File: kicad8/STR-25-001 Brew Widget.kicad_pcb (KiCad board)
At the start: 4 copper layers, 25 x 94 mm, 71 parts, among them J1 USB_B_Micro, Q1 IRLML6401, Q2 FS8205A, SW1 BOOT, SW2 RESET, U1 ESP32-C3-MINI-1-N4, U2 TP4057, U3 MT3608, U4 MPU-6500, U5 MAX17048, U6 DS18B20U, U7 DW01A

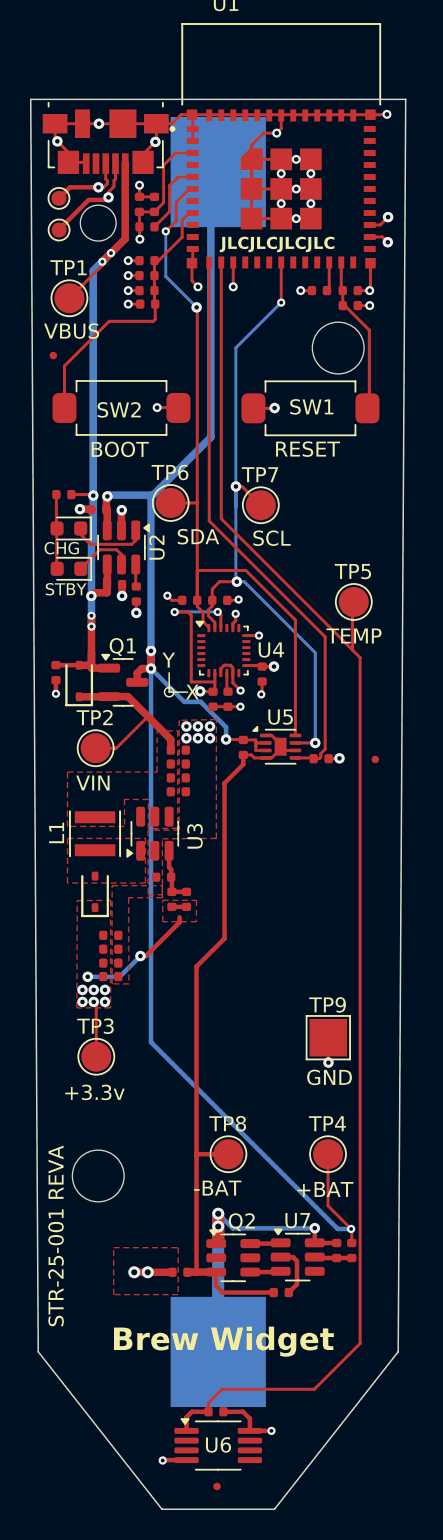
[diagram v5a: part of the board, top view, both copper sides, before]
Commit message: Finalising deisgn, first checks review done
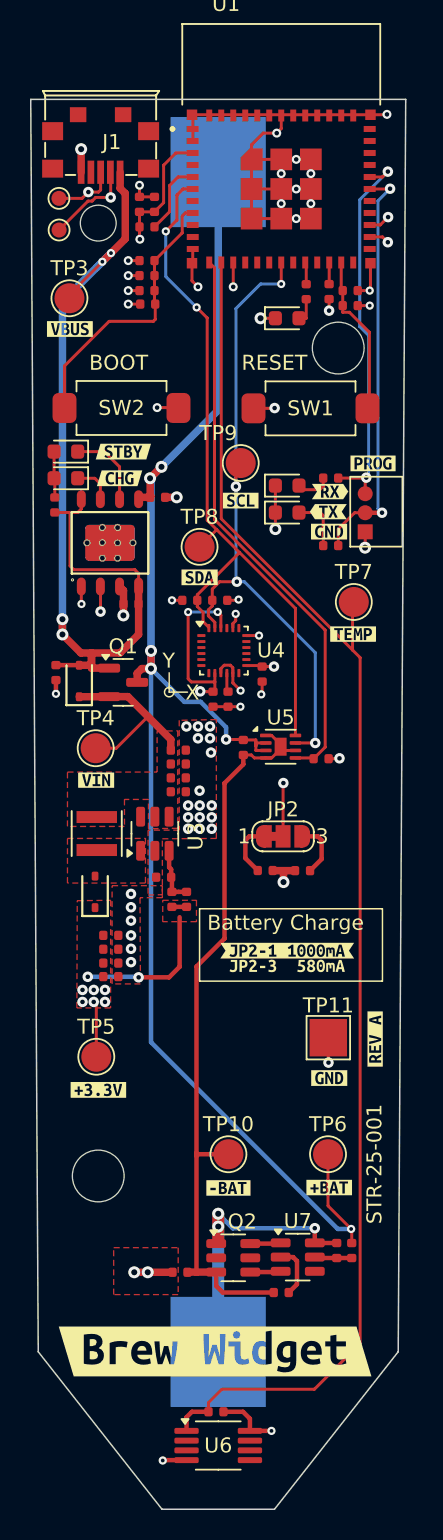
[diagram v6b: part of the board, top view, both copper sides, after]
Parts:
- removed FID1, FID2, FID3: Fiducial, Fiducial:Fiducial_0.5mm_Mask1mm
- removed PN1: ~, JLCPCB-Kicad-Footprints:Part_Num_JLCPCB
- added D5: RED, LED_SMD:LED_0603_1608Metric, F.Cu at (149.1, 85.3)
- added D6: RED, LED_SMD:LED_0603_1608Metric, F.Cu at (149.1, 96.5)
- added D7: RED, LED_SMD:LED_0603_1608Metric, F.Cu at (149.1, 98.3)
- added JP2: SolderJumper_3_Bridged12, Jumper:SolderJumper-3_P1.3mm_Bridged12_RoundedPad1.0x1.5mm_NumberLabels, F.Cu at (148.8, 119.9)
- added PROG1: Pogo Pin 1.27mm, STR-Footprints:PROG_1x3_1.27, F.Cu at (154.3, 99.6)
- added R18: 1.2kΩ, JLCPCB-Kicad-Footprints:R_0402, F.Cu at (147.6, 122.2)
- added R19: 1.5kΩ, JLCPCB-Kicad-Footprints:R_0402, F.Cu at (150.4, 83.6)
- added R20: 1.5kΩ, JLCPCB-Kicad-Footprints:R_0402, F.Cu at (152.0, 96.0)
- added R21: 1.5kΩ, JLCPCB-Kicad-Footprints:R_0402, F.Cu at (152.0, 100.5)
- added kibuzzard-67834543: G***, kibuzzard-67834543, F.Cu at (151.9, 136.0)
- added kibuzzard-67834564: G***, kibuzzard-67834564, F.Cu at (136.5, 136.8)
- added kibuzzard-6783457B: G***, kibuzzard-6783457B, F.Cu at (151.9, 143.3)
- added kibuzzard-67834594: G***, kibuzzard-67834594, F.Cu at (145.2, 143.3)
- added kibuzzard-678345AF: G***, kibuzzard-678345AF, F.Cu at (153.5, 106.4)
- added kibuzzard-678345CB: G***, kibuzzard-678345CB, F.Cu at (136.4, 116.1)
- added kibuzzard-678345D9: G***, kibuzzard-678345D9, F.Cu at (143.3, 102.6)
- added kibuzzard-678345E8: G***, kibuzzard-678345E8, F.Cu at (146.0, 97.5)
- added kibuzzard-67834607: G***, kibuzzard-67834607, F.Cu at (134.6, 86.1)
- added kibuzzard-678346A0: G***, kibuzzard-678346A0, F.Cu at (144.3, 154.2)
- added kibuzzard-67834787: G***, kibuzzard-67834787, F.Cu at (155.0, 133.4)
- added kibuzzard-67835DB7: G***, kibuzzard-67835DB7, F.Cu at (151.9, 99.6)
- added kibuzzard-67835E03: G***, kibuzzard-67835E03, F.Cu at (152.0, 96.9)
- added kibuzzard-67835E0F: G***, kibuzzard-67835E0F, F.Cu at (151.8, 98.2)
- added kibuzzard-67835E3B: G***, kibuzzard-67835E3B, F.Cu at (154.8, 95.0)
- added kibuzzard-67836539: G***, kibuzzard-67836539, F.Cu at (138.2, 94.2)
- added kibuzzard-67836544: G***, kibuzzard-67836544, F.Cu at (137.9, 96.0)
- added kibuzzard-67837AE8: G***, kibuzzard-67837AE8, F.Cu at (149.1, 127.5)
- added kibuzzard-67837E72: G***, kibuzzard-67837E72, F.Cu at (149.1, 128.5)
- C11: value 4.7uF -> 10uF
- J1: footprint Connector_USB:USB_Micro-B_Molex_47346-0001 -> STR-Footprints:MICRO-USB-SMD_5P_C40945
- L1: footprint STR-Passive:IND_LQH3NPZ220MMEL -> STR-Footprints:IND_LQH3NPZ220MMEL
- SW1, SW2: footprint STR-Switch:SW_SMD_SPST_8x3.6 -> STR-Footprints:SW_SMD_SPST_8x3.6
- U1: footprint STR-ESP32:ESP32-C3-MINI-1-N4 -> STR-Footprints:ESP32-C3-MINI-1-N4
- U2: value TP4057 -> TP4056; footprint Package_TO_SOT_SMD:TSOT-23-6 -> STR-Footprints:ESOP-8_L4.9-W3.9-P1.27-LS6.0-BL-EP
- moved R10 21.5 mm to (150.1, 122.2), turned to 180 degrees
- moved D3 7.82 mm to (134.3, 94.2)
- moved C15 4.01 mm to (140.5, 97.3), turned to 0 degrees
- moved TP8 3.50 mm to (143.3, 100.6)
- moved D2 3.35 mm to (134.3, 96.0)
- moved TP9 3.12 mm to (146.0, 95.0)
- moved C11 1.70 mm to (138.7, 104.4), turned to 180 degrees
- moved R9 0.92 mm to (133.6, 97.8), turned to 90 degrees
- moved U2 0.83 mm to (137.3, 100.3), turned to 0 degrees
- moved R7 0.65 mm to (151.9, 83.6), turned to 90 degrees
- moved J1 0.36 mm to (136.7, 73.7), turned to -90 degrees
- moved L1 0.11 mm to (136.4, 119.7)
- renumbered TP11 to TP1, TP8 to TP10, TP9 to TP11, TP10 to TP2, TP1 to TP3, TP2 to TP4, TP3 to TP5, TP4 to TP6, TP5 to TP7, TP6 to TP8, TP7 to TP9
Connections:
- D2 pad 1: Net-(D2-K) -> /~{CHG}
- D3 pad 1: Net-(D3-K) -> /~{STBY}
- R10 pad 1: Net-(U2-PROG) -> Net-(JP2-B)
- U1 pad 20: unconnected-(U1-IO6-Pad20) -> GPIO6
- U1 pad 30: unconnected-(U1-IO20/RXD0-Pad30) -> TX_IN
- U1 pad 31: unconnected-(U1-IO21/TXD0-Pad31) -> RX_IN
- U2 pad 1: Net-(D2-K) -> GND
- U2 pad 2: GND -> /PROG
- U2 pad 3: +BATT -> GND
- U2 pad 5: Net-(D3-K) -> +BATT
- U2 pad 6: Net-(U2-PROG) -> /~{STBY}
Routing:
- net TX_IN: track 0.00 -> 27.9 mm, vias 0 -> 2
- net RX_IN: track 0.00 -> 25.8 mm, vias 0 -> 2
- net /PROG: track 0.00 -> 24.5 mm, vias 0 -> 2
- net VBUS: track 49.5 -> 64.8 mm, vias 6 -> 4
- net GND: track 91.0 -> 82.6 mm, vias 40 -> 57
- net /~{STBY}: track 0.00 -> 5.37 mm
- net Net-(D2-K): track 5.12 -> 0.00 mm
- net Net-(D3-K): track 4.03 -> 0.00 mm
- net Net-(JP2-B): track 0.00 -> 3.73 mm
- net Net-(D7-A): track 0.00 -> 3.70 mm
- net Net-(JP2-A): track 0.00 -> 3.68 mm
- net /~{CHG}: track 0.00 -> 2.69 mm
- net Net-(D6-A): track 0.00 -> 2.26 mm
- net +BATT: track 105.2 -> 103.0 mm, vias 5 -> 6
- net Net-(D2-A): track 4.99 -> 3.08 mm
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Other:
- board text added: "Battery Charge"
- board text added: "STR-25-001"
- board text removed: "+3.3v"
- board text removed: "+BAT"
- board text removed: "-"
- board text removed: "-BAT"
- board text removed: "Brew Widget"
- board text removed: "CHG"
- board text removed: "GND"
- board text removed: "SCL"
- board text removed: "SDA"
- board text removed: "STBY"
- board text removed: "STR-25-001 REVA"
- board text removed: "TEMP"
- board text removed: "VBUS"
- board text removed: "VIN"

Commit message: BOM generated
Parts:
- removed the R16 at (141.9, 148.9)
- added R20: 0Ω, JLCPCB-Kicad-Footprints:R_0805, F.Cu at (141.3, 149.0)
- D5: renamed from D2; value CHG -> RED
- D6: renamed from D3; value STBY -> GREEN
- SW1: value BOOT -> SPST 8x3.6
- SW2: value RESET -> SPST 8x3.6
- moved D5 0.56 mm to (134.9, 96.0)
- moved D6 0.56 mm to (134.9, 94.2)
- moved R12 0.41 mm to (134.0, 97.9)
- moved kibuzzard-67836539 0.33 mm to (138.5, 94.2)
- moved kibuzzard-67836544 0.30 mm to (138.2, 95.9)
- renumbered C11 to C10, C10 to C11, D6 to D1, D5 to D2, D7 to D3, D1 to D4, D4 to D7, JP2 to JP1, R21 to R10, R8 to R11, R9 to R12, R18 to R13, R10 to R14, R11 to R15, R12 to R16, R13 to R17, R14 to R18, R15 to R19, R17 to R21, R20 to R5, R5 to R6, R6 to R7, R19 to R8, R7 to R9
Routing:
- net GND: track 82.6 -> 80.0 mm, vias 57 -> 63
- net /~{STBY}: track 5.37 -> 4.82 mm
- net /~{CHG}: track 2.69 -> 2.14 mm

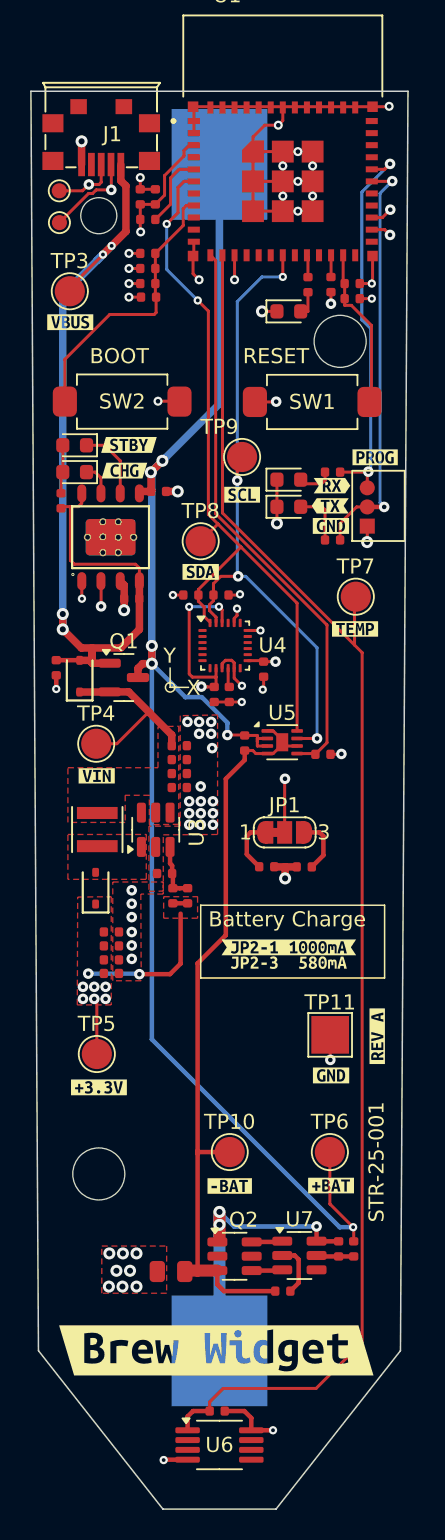
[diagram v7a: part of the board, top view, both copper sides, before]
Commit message: Changed to Buck Regulator using MT3406 Changed from DW01A on battery protection to AP9101C due to better low voltage protection
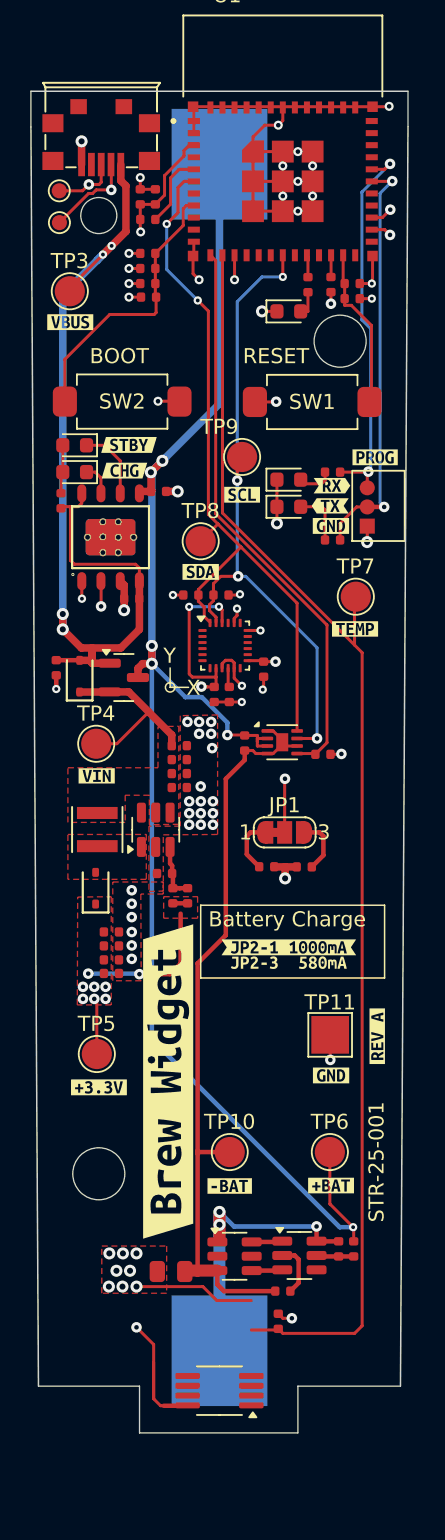
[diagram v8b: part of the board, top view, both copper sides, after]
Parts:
- moved kibuzzard-678346A0 18.1 mm to (141.1, 136.4), turned to 90 degrees
- moved R18 7.20 mm to (148.4, 152.3), turned to -90 degrees
- moved U6 3.60 mm to (144.5, 156.9), turned to 180 degrees
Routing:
- net TEMP: track 94.2 -> 85.8 mm
- net +3.3V: track 45.4 -> 52.2 mm, vias 21 -> 22
- net GND: track 80.0 -> 86.4 mm, vias 63 -> 62
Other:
- board size 25 x 94 mm -> 25 x 88.9 mm
